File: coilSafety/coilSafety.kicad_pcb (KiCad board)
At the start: 2 copper layers, 99.1 x 99.1 mm, 22 parts, among them J1 PJ-037BH, J10 Conn_01x02_Pin, J11 Conn_01x02_Pin, J2 Screw_Terminal_01x08, J3 Screw_Terminal_01x02, J4 Screw_Terminal_01x02, J5 Screw_Terminal_01x06, J6 Screw_Terminal_01x02, J7 Conn_01x01_Pin, J8 Conn_01x08_Pin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

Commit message: Working on PCB
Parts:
- removed J7: Conn_01x01_Pin, Connector_Samtec_HPM_THT:Samtec_HPM-01-01-x-S_Straight_1x01_Pitch5.08mm
- removed J8: Conn_01x08_Pin, Connector_PinHeader_2.54mm:PinHeader_1x08_P2.54mm_Vertical
- J1, R1, R2, R3, R4: moved to F.Cu
- J10, J11, J9: footprint Connector_PinHeader_2.54mm:PinHeader_1x02_P2.54mm_Vertical -> TerminalBlock:TerminalBlock_bornier-2_P5.08mm
- M1: value ~ -> ESP32-C6-DevKitM-1
- U1, U2: value ~ -> AZDC007-1AE-12D
- moved J11 132.0 mm to (111.5, 70.0)
- moved J4 120.9 mm to (106.0, 57.0)
- moved PS2 105.2 mm to (132.3, 80.4), turned to 180 degrees
- moved U2 95.8 mm to (132.8, 64.0)
- moved PS3 94.4 mm to (132.0, 142.0), turned to -90 degrees
- moved J9 93.7 mm to (105.5, 133.0), turned to 0 degrees
- moved K1 50.5 mm to (172.0, 140.4), turned to 90 degrees
- moved J2 46.9 mm to (108.0, 126.0)
- moved J6 45.2 mm to (195.0, 141.0), turned to -90 degrees
- moved J5 43.8 mm to (195.0, 94.0)
- moved J3 38.6 mm to (154.5, 56.8)
- moved R4 36.8 mm to (131.0, 116.0), turned to 180 degrees
- moved R3 36.3 mm to (131.0, 110.0), turned to 180 degrees
- moved R2 36.1 mm to (131.0, 104.0), turned to 180 degrees
- moved R1 36.0 mm to (131.0, 98.0), turned to 180 degrees
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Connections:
- J1 pad 1: Net-(J9-Pin_2) -> Net-(J6-Pin_1)
- J1 pad 2: Net-(J6-Pin_2) -> Net-(J9-Pin_1)
- J9 pad 1: Net-(J6-Pin_1) -> Net-(J9-Pin_1)
- J9 pad 2: Net-(J9-Pin_2) -> Net-(J6-Pin_1)
- K1 pad 1: Net-(J9-Pin_2) -> Net-(J9-Pin_1)
- K1 pad 3: Net-(J7-Pin_1) -> Net-(J6-Pin_2)
- K1 pad 4: Net-(J6-Pin_1) -> Net-(J9-Pin_1)
- M1 pad 10: Net-(J2-Pin_2) -> Net-(M1-GPIO_6)
- M1 pad 22: Net-(J8-Pin_7) -> unconnected-(M1-GPIO_18-Pad22)
- M1 pad 23: Net-(J8-Pin_8) -> unconnected-(M1-GPIO_19-Pad23)
- M1 pad 3: unconnected-(M1-GPIO_2-Pad3) -> Net-(J2-Pin_8)
- M1 pad 30: Net-(PS1--VIN) -> GND
- M1 pad 4: unconnected-(M1-GPIO_3-Pad4) -> Net-(J2-Pin_6)
- M1 pad 5: unconnected-(M1-GPIO_4-Pad5) -> Net-(J2-Pin_4)
- M1 pad 6: Net-(J2-Pin_8) -> Net-(J2-Pin_2)
- M1 pad 7: Net-(J2-Pin_6) -> unconnected-(M1-GPIO_0-Pad7)
- M1 pad 8: Net-(J2-Pin_4) -> unconnected-(M1-GPIO_1-Pad8)
- PS1 pad 1: Net-(PS1--VIN) -> GND
- PS2 pad 1: Net-(PS1--VIN) -> GND
- PS3 pad 2: +3.3V -> Net-(M1-GPIO_6)
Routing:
- net GND: track 169.9 -> 0.00 mm, vias 2 -> 0
- net +3.3V: track 130.2 -> 0.00 mm
- net +5V: track 25.8 -> 139.6 mm
- net Net-(J5-Pin_6): track 122.1 -> 33.1 mm
- net Net-(J6-Pin_2): track 85.0 -> 0.00 mm
- net Net-(J9-Pin_2): track 82.2 -> 0.00 mm
- net Net-(PS2-+VOUT): track 76.2 -> 0.00 mm, vias 1 -> 0
- net Net-(PS2--VOUT): track 66.7 -> 0.00 mm
- net Net-(J6-Pin_1): track 63.9 -> 0.00 mm
- net Net-(PS1--VOUT): track 62.8 -> 0.00 mm, vias 2 -> 0
- net Net-(PS1-+VOUT): track 58.0 -> 0.00 mm, vias 2 -> 0
- net Net-(M1-GPIO_22): track 56.9 -> 0.00 mm, vias 1 -> 0
- net Net-(PS1--VIN): track 52.0 -> 0.00 mm
- net Net-(J11-Pin_2): track 48.0 -> 0.00 mm
- net Net-(J10-Pin_1): track 42.0 -> 0.00 mm
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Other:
- board size 99.1 x 99.1 mm -> 98 x 98 mm
- board text removed: "12v"
- board text removed: "3.3v"
- board text removed: "Coil In 1"
- board text removed: "Coil In 2"
- board text removed: "Coil Relay"
- board text removed: "D1"
- board text removed: "D2"
- board text removed: "DC to DC Voltage"
- board text removed: "Dr. Biedermann Electromagnet Safety Circuit"
- board text removed: "ESP32 Microcontroller"
- board text removed: "Extra Output"
- board text removed: "GND"
- board text removed: "Made By: Jackson McDowell"
- board text removed: "Max Coil Current 15A Max Coil Voltage 65v"
- board text removed: "Pump In"
- board text removed: "Pump Out"
- board text removed: "Pump Relay"
- board text removed: "Short"
- board text removed: "Water Sensors"

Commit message: final commit
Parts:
- added REF**: MountingHole_4.3mm_M4, MountingHole:MountingHole_4.3mm_M4, F.Cu at (108.0, 83.0)
- added REF**: MountingHole_4.3mm_M4, MountingHole:MountingHole_4.3mm_M4, F.Cu at (125.0, 144.0)
- added REF**: MountingHole_4.3mm_M4, MountingHole:MountingHole_4.3mm_M4, F.Cu at (194.0, 83.0)
- added REF**: MountingHole_4.3mm_M4, MountingHole:MountingHole_4.3mm_M4, F.Cu at (194.0, 144.0)
- M1: value ESP32-C6-DevKitM-1 -> ESP32-C6-DevKitM-1_1
- moved J6 13.0 mm to (195.0, 128.0)
- moved K1 9.00 mm to (172.0, 131.4)
- moved PS3 5.10 mm to (137.0, 143.0)
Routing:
- net Net-(M1-GPIO_6): track 0.00 -> 125.5 mm
- net Net-(PS3--VOUT): track 0.00 -> 110.6 mm
- net Net-(J6-Pin_1): track 0.00 -> 102.7 mm
- net Net-(J9-Pin_1): track 0.00 -> 99.9 mm
- net +3.3V: track 0.00 -> 75.8 mm
- net Net-(J11-Pin_1): track 0.00 -> 53.4 mm
- net Net-(J10-Pin_1): track 0.00 -> 52.9 mm
- net Net-(J10-Pin_2): track 0.00 -> 47.2 mm
- net Net-(M1-GPIO_22): track 0.00 -> 46.1 mm
- net Net-(J11-Pin_2): track 0.00 -> 43.4 mm
- net Net-(PS3-+VOUT): track 0.00 -> 42.3 mm
- net Net-(M1-GPIO_23): track 0.00 -> 32.8 mm
- net +5V: track 139.6 -> 165.5 mm
- net Net-(PS2--VOUT): track 0.00 -> 18.7 mm
- net Net-(PS1--VOUT): track 0.00 -> 18.0 mm
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- added copper zone on B.Cu, net GND
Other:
- board text added: "Coil 1"
- board text added: "Coil 2"
- board text added: "Jackson McDowell 07/16/2024"
- board text added: "Moisture Sensor"
- board text added: "Pump In"
- board text added: "Pump Out"
- board text added: "Thermistor"

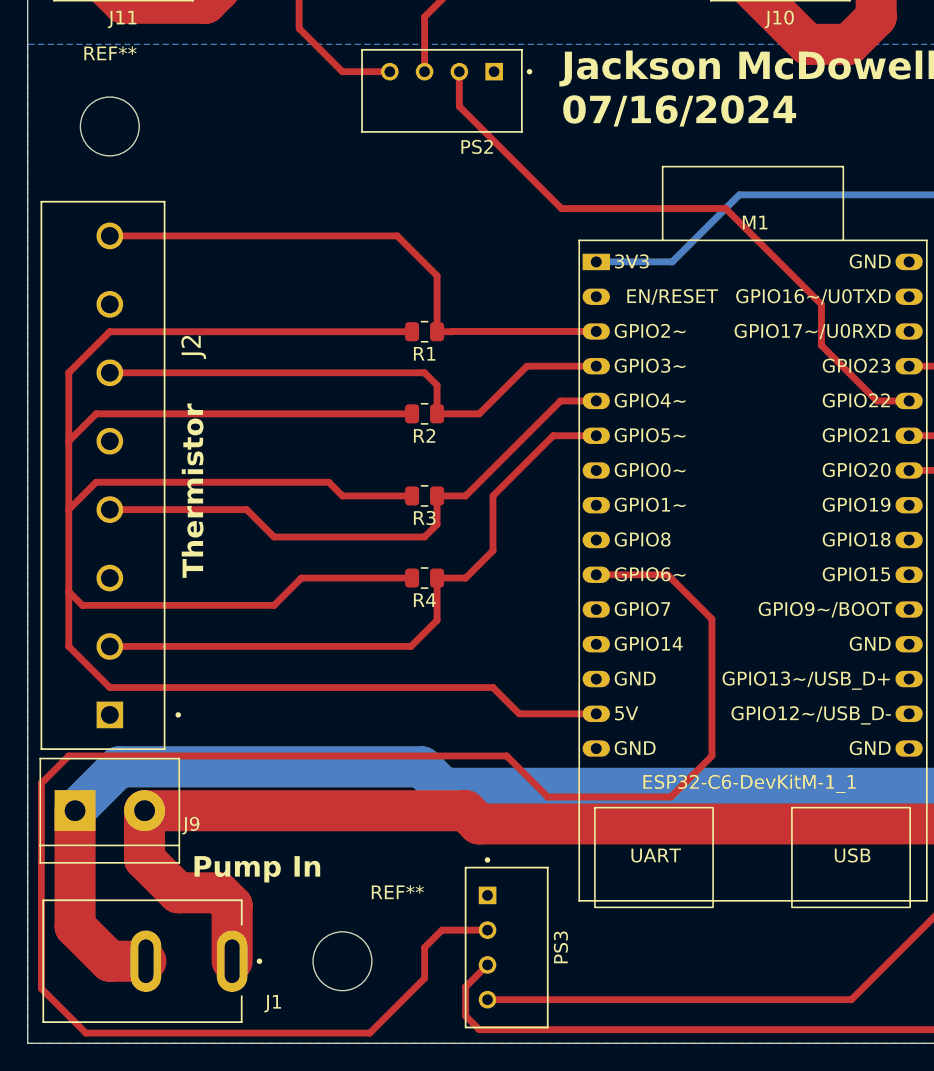
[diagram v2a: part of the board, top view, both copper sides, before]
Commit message: fixed trace and text
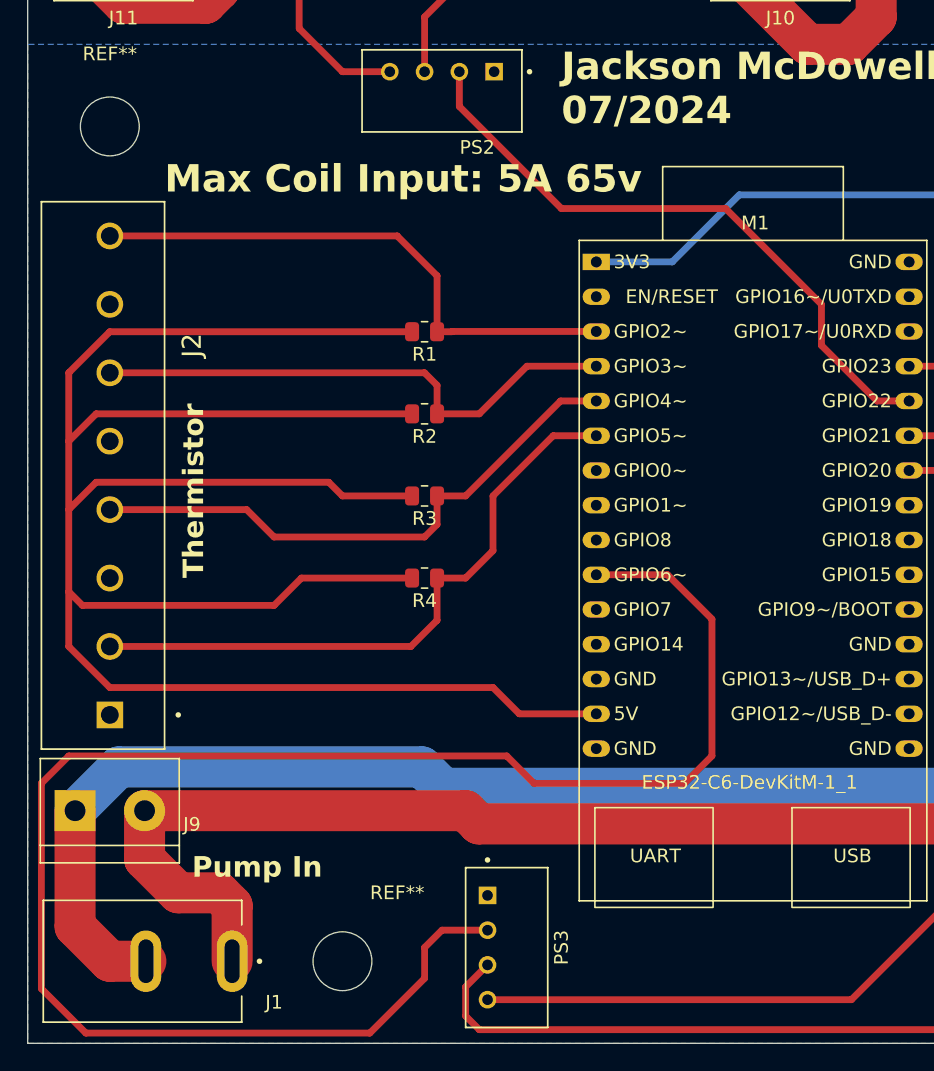
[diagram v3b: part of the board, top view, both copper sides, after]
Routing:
- net Net-(M1-GPIO_6): track 125.5 -> 124.7 mm
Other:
- board text added: "Jackson McDowell 07/2024"
- board text added: "Max Coil Input: 5A 65v"
- board text removed: "Jackson McDowell 07/16/2024"
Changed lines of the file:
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@@
 		(layer "Edge.Cuts")
 	)
-	(gr_text "Jackson McDowell \n07/16/2024"
+	(gr_text "Jackson McDowell \n07/2024"
 		(at 141 83 0)
 		(layer "F.SilkS")
@@
 		)
 	)
+	(gr_text "Max Coil Input: 5A 65v"
+		(at 112 88 0)
+		(layer "F.SilkS")
+		(effects
+			(font
+				(size 2 2)
+				(thickness 0.5)
+				(bold yes)
+			)
+			(justify left bottom)
+		)
+	)
 	(gr_text "Pump In"
 		(at 114 138 0)
@@
 	)
 	(gr_text_box "Coil Safety Circuit\nBiedermann Lab\nv2\n"
-		(start 171.5 90.0682)
-		(end 183.5 126.6016)
+		(start 169 85.4666)
+		(end 181 122)
 		(angle 90)
-		(layer "B.SilkS")
+		(layer "F.SilkS")
 		(effects
 			(font
@@
 				(thickness 0.3)
 			)
-			(justify left top mirror)
+			(justify left top)
 		)
 		(border yes)
@@
 	)
 	(segment
+		(start 139 131)
+		(end 150 131)
+		(width 0.5)
+		(layer "F.Cu")
+		(net 25)
+	)
+	(segment
+		(start 103 146)
+		(end 103 131)
+		(width 0.5)
+		(layer "F.Cu")
+		(net 25)
+	)
+	(segment
+		(start 106.25 149.25)
+		(end 103 146)
+		(width 0.5)
+		(layer "F.Cu")
+		(net 25)
+	)
+	(segment
+		(start 148.76026 115.76026)
+		(end 143.546 115.76026)
+		(width 0.5)
+		(layer "F.Cu")
+		(net 25)
+	)
+	(segment
+		(start 132.27 141.73)
+		(end 131 143)
+		(width 0.5)
+		(layer "F.Cu")
+		(net 25)
+	)
+	(segment
+		(start 105 129)
+		(end 137 129)
+		(width 0.5)
+		(layer "F.Cu")
+		(net 25)
+	)
+	(segment
+		(start 150 131)
+		(end 152 129)
+		(width 0.5)
+		(layer "F.Cu")
+		(net 25)
+	)
+	(segment
+		(start 137 129)
+		(end 139 131)
+		(width 0.5)
+		(layer "F.Cu")
+		(net 25)
+	)
+	(segment
+		(start 103 131)
+		(end 105 129)
+		(width 0.5)
+		(layer "F.Cu")
+		(net 25)
+	)
+	(segment
+		(start 131 143)
+		(end 131 145.25)
+		(width 0.5)
+		(layer "F.Cu")
+		(net 25)
+	)
+	(segment
+		(start 152 119)
+		(end 148.76026 115.76026)
+		(width 0.5)
+		(layer "F.Cu")
+		(net 25)
+	)
+	(segment
+		(start 135.6 141.73)
+		(end 132.27 141.73)
+		(width 0.5)
+		(layer "F.Cu")
+		(net 25)
+	)
+	(segment
+		(start 152 129)
+		(end 152 119)
+		(width 0.5)
+		(layer "F.Cu")
+		(net 25)
+	)
+	(segment
 		(start 131 145.25)
-		(end 131 143)
-		(width 0.5)
-		(layer "F.Cu")
-		(net 25)
-	)
-	(segment
-		(start 105 129)
-		(end 103 131)
-		(width 0.5)
-		(layer "F.Cu")
-		(net 25)
-	)
-	(segment
-		(start 149 132)
-		(end 140 132)
-		(width 0.5)
-		(layer "F.Cu")
-		(net 25)
-	)
-	(segment
-		(start 103 131)
-		(end 103 146)
-		(width 0.5)
-		(layer "F.Cu")
-		(net 25)
-	)
-	(segment
-		(start 152 119)
-		(end 152 129)
-		(width 0.5)
-		(layer "F.Cu")
-		(net 25)
-	)
-	(segment
-		(start 137 129)
-		(end 105 129)
-		(width 0.5)
-		(layer "F.Cu")
-		(net 25)
-	)
-	(segment
-		(start 140 132)
-		(end 137 129)
-		(width 0.5)
-		(layer "F.Cu")
-		(net 25)
-	)
-	(segment
-		(start 148.76026 115.76026)
-		(end 152 119)
-		(width 0.5)
-		(layer "F.Cu")
-		(net 25)
-	)
-	(segment
-		(start 131 143)
-		(end 132.27 141.73)
-		(width 0.5)
-		(layer "F.Cu")
-		(net 25)
-	)
-	(segment
-		(start 143.546 115.76026)
-		(end 148.76026 115.76026)
+		(end 127 149.25)
 		(width 0.5)
 		(layer "F.Cu")
@@
 	(segment
 		(start 127 149.25)
-		(end 131 145.25)
-		(width 0.5)
-		(layer "F.Cu")
-		(net 25)
-	)
-	(segment
-		(start 132.27 141.73)
-		(end 135.6 141.73)
-		(width 0.5)
-		(layer "F.Cu")
-		(net 25)
-	)
-	(segment
-		(start 103 146)
 		(end 106.25 149.25)
 		(width 0.5)
 		(layer "F.Cu")
-		(net 25)
-	)
-	(segment
-		(start 106.25 149.25)
-		(end 127 149.25)
-		(width 0.5)
-		(layer "F.Cu")
-		(net 25)
-	)
-	(segment
-		(start 152 129)
-		(end 149 132)
-		(width 0.5)
-		(layer "F.Cu")
